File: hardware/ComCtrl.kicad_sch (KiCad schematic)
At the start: 8 parts, among them K10 G5V-2-DC12, K11 G5V-2-DC12, U9 ILD74

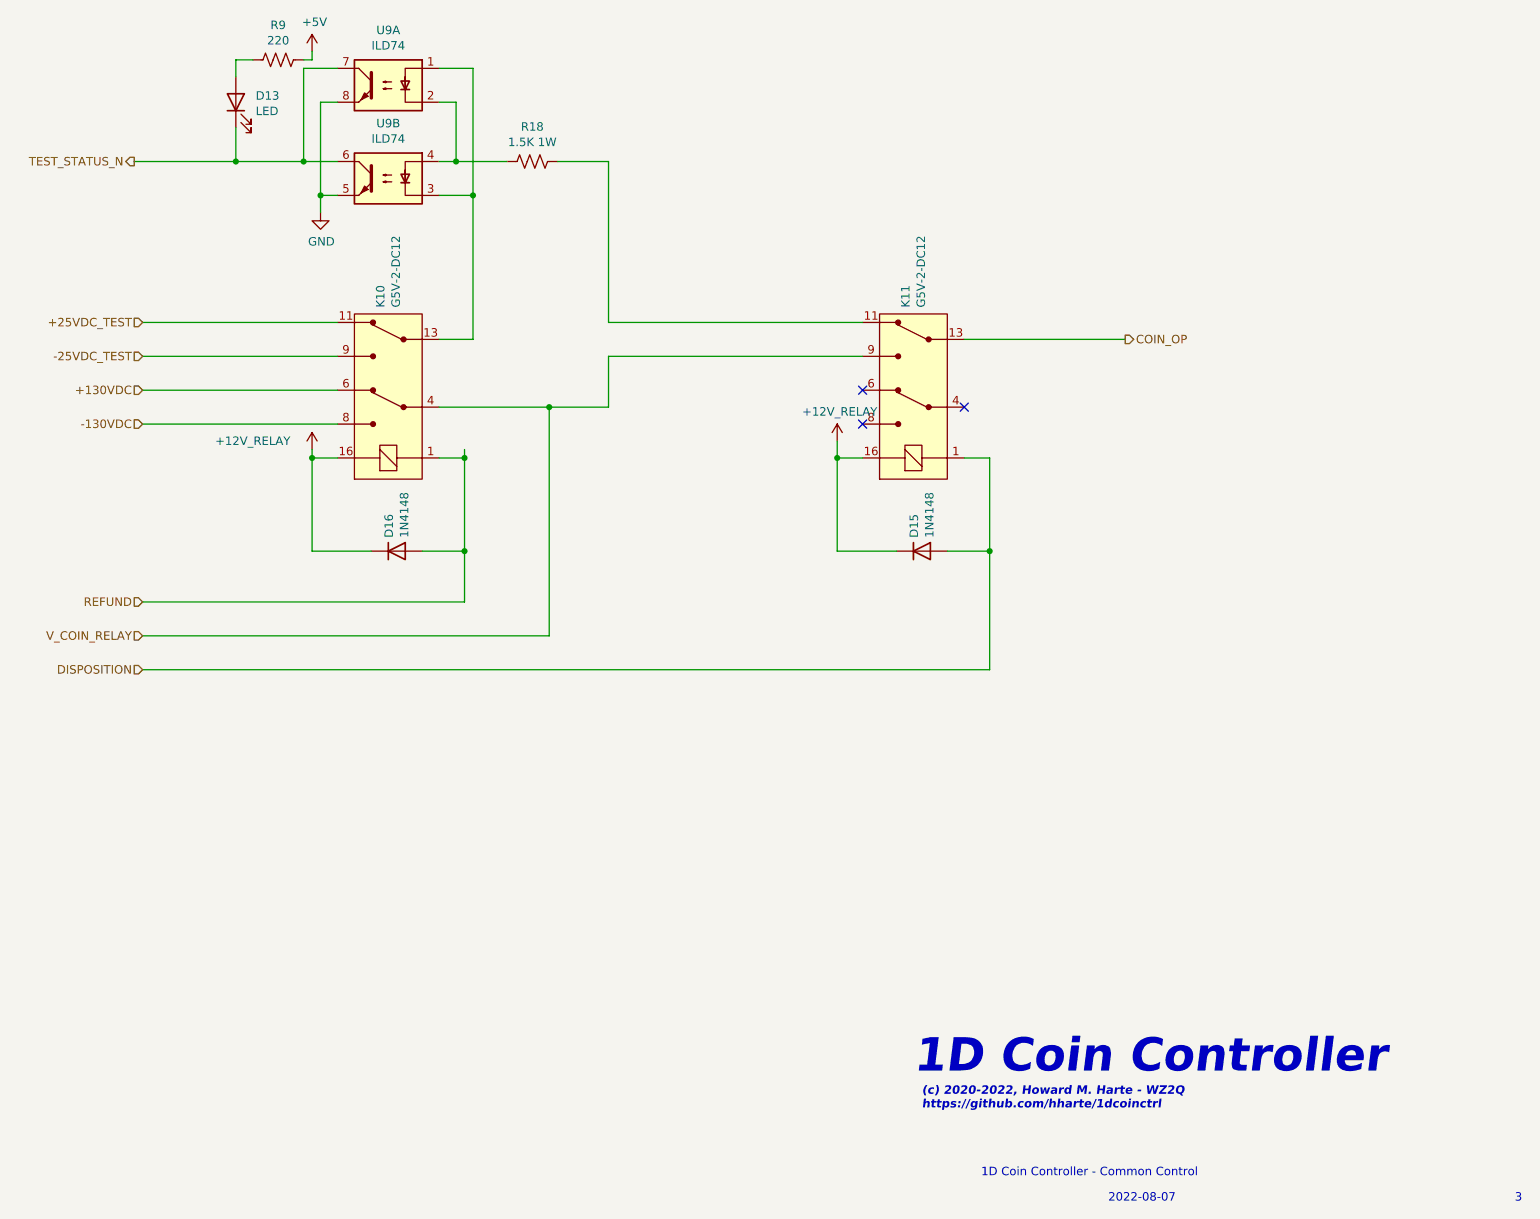
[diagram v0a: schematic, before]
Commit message: Issue 4: Switch from PIC to AVR128DA28 MCU.
    * The AVR128DA28 is supported by the Arduino IDE.
    * Simpler UPDI programming.
    * Update to KiCAD 8.0.1
    * Fix footprint outline for IA1224S DC-DC converter.
    * Add initial Arduino firmware for AVR128DA28 MCU.
    * Move Earth Ground hole.
    * Add jumpers for UART and UPDI configuration.
    * Add 3D-printable end caps for Hammond enclosure.
    * Geographical reannotate PCB.
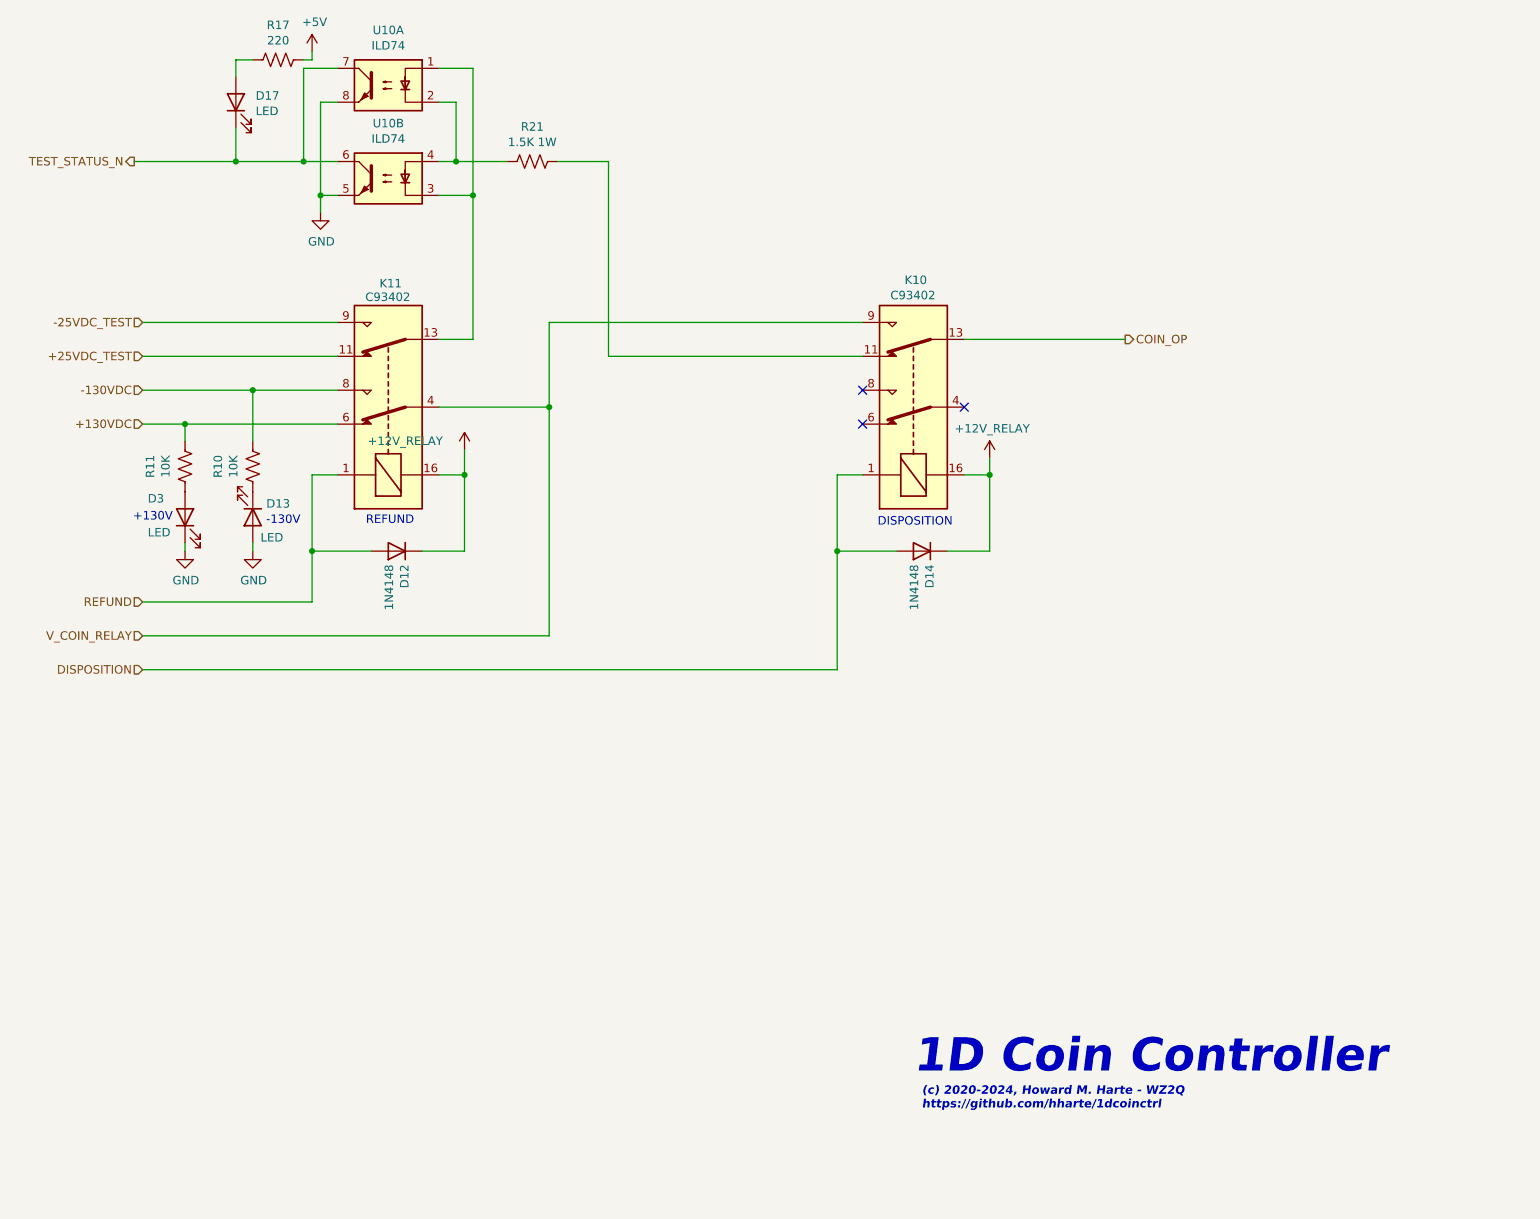
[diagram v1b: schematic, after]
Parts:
- added D13, D3: LED, LED_THT:LED_D5.0mm, symbol Device:LED
- added R10, R11: 10K, Resistor_THT:R_Axial_DIN0207_L6.3mm_D2.5mm_P7.62mm_Horizontal, symbol Device:R_US
- D12: renamed from D16; Digi-Key_PN (none) -> 1N4148TACT-ND; MPN (none) -> 1N4148TA
- D14: renamed from D15; Digi-Key_PN (none) -> 1N4148TACT-ND; MPN (none) -> 1N4148TA
- D17: renamed from D13; Digi-Key_PN (none) -> 1497-1031-ND; MPN (none) -> XLUR12D
- K10: renamed from K11; value G5V-2-DC12 -> C93402; footprint digikey-footprints:Relay_THT_G5V-2 -> Relay_THT:Relay_DPDT_Omron_G5V-2; symbol 1d_coinctrl_r2-rescue:G5V-2-DC12-dk_Signal-Relays-Up-to-2-Amps -> Relay:G5V-2; DK_Datasheet_Link http://omronfs.omron.com/en_US/ecb/products/pdf/en-g5v_2.pdf -> https://omronfs.omron.com/en_US/ecb/products/pdf/en-g5v_2.p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; Digi-Key_PN Z768-ND -> PB1125-ND; MPN G5V-2-DC12 -> C93402
- K11: renamed from K10; value G5V-2-DC12 -> C93402; footprint digikey-footprints:Relay_THT_G5V-2 -> Relay_THT:Relay_DPDT_Omron_G5V-2; symbol 1d_coinctrl_r2-rescue:G5V-2-DC12-dk_Signal-Relays-Up-to-2-Amps -> Relay:G5V-2; DK_Datasheet_Link http://omronfs.omron.com/en_US/ecb/products/pdf/en-g5v_2.pdf -> https://omronfs.omron.com/en_US/ecb/products/pdf/en-g5v_2.p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; Digi-Key_PN Z768-ND -> PB1125-ND; MPN G5V-2-DC12 -> C93402
- R17: renamed from R9; Digi-Key_PN (none) -> S220HCT-ND; MPN (none) -> CFM12JT220R
- R21: renamed from R18; Digi-Key_PN (none) -> PPC1.5KW-1CT-ND; MPN (none) -> PR01000101501JR500
- U10: renamed from U9; Digi-Key_PN (none) -> CNY74-2H-ND; MPN (none) -> CNY74-2H
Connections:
- net +130VDC: now also R11.1
- net -130VDC: now also R10.1
- net GND: now also D13.2 (A), D3.1 (K)
- new net: D13.1 (K), R10.2
- new net: D3.2 (A), R11.2
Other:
- note added: "(c) 2020-2024, Howard M. Harte - WZ2Q https://github.com/hharte/1dcoinctrl"
- note added: "+130V"
- note added: "-130V"
- note added: "DISPOSITION"
- note added: "REFUND"
- note removed: "(c) 2020-2022, Howard M. Harte - WZ2Q https://github.com/hharte/1dcoinctrl"
- note removed: "1D Coin Controller - Common Control"
- note removed: "2022-08-07"
- note removed: "3"
- title: (none) -> 1D Coin Controller - Common Control
- moved on the sheet: D12, D14
